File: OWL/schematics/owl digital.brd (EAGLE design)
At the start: 60 x 57 mm, 60 parts, among them IC1 REG1117, IC3 IS61WV51216BLL-10TLI, U2 WM8731, U4 STM32F405ZGT6

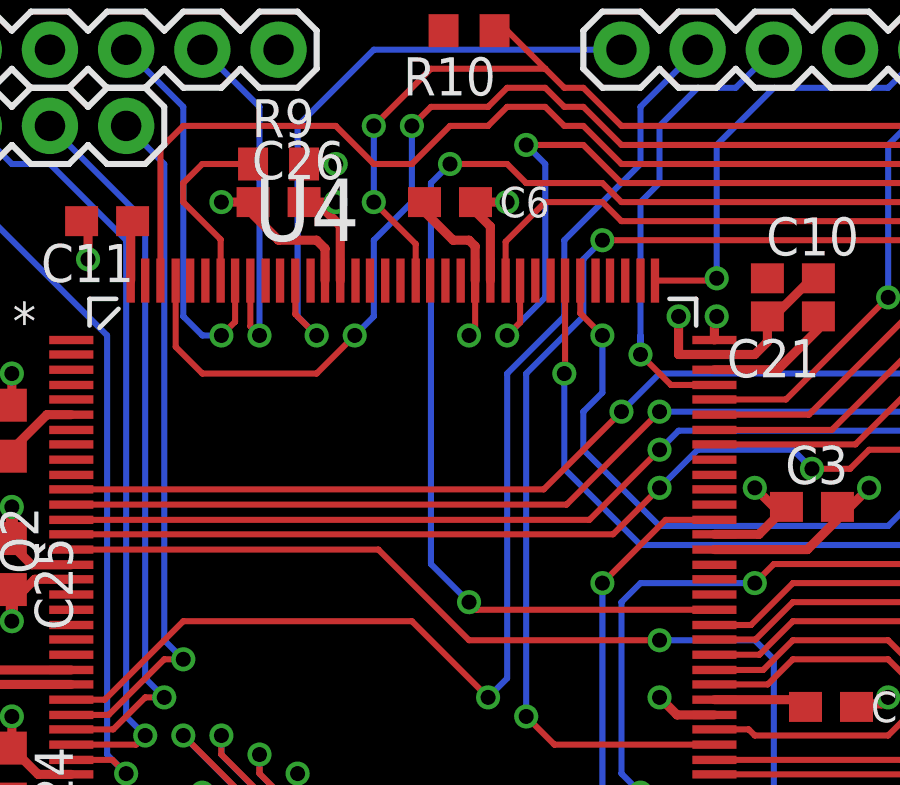
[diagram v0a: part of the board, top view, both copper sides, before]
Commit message: split owl board into analog and digital boards
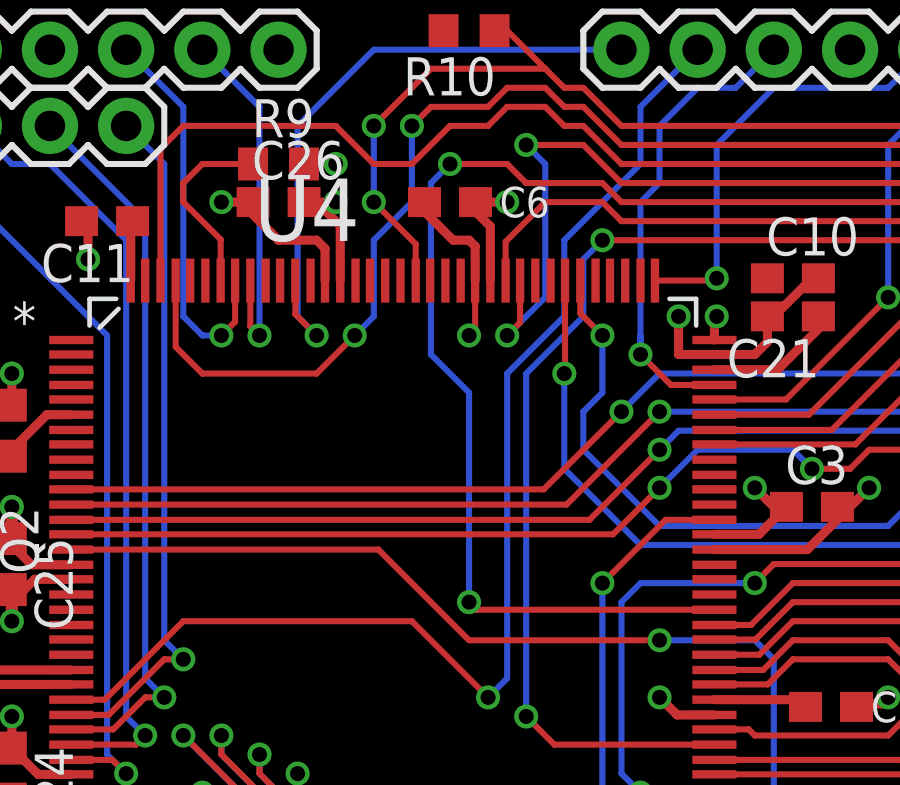
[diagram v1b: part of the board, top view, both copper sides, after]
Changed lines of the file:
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@@
 <contactref element="PWR" pad="3"/>
 <wire x1="19.05" y1="6.35" x2="19.05" y2="4.475" width="0.8128" layer="1"/>
-<wire x1="30.265" y1="47.625" x2="38.1" y2="55.245" width="0" layer="19" extent="1-1"/>
+<wire x1="18.415" y1="3.84" x2="16.54" y2="3.84" width="0.8128" layer="1"/>
+<wire x1="16.54" y1="3.84" x2="16.51" y2="3.81" width="0.8128" layer="1"/>
+<via x="16.51" y="3.81" extent="1-16" drill="0.5"/>
+<wire x1="10.1346" y1="3.8354" x2="12.0396" y2="3.8354" width="0.8128" layer="1"/>
+<wire x1="12.0396" y1="3.8354" x2="12.065" y2="3.81" width="0.8128" layer="1"/>
+<via x="12.065" y="3.81" extent="1-16" drill="0.5"/>
 <wire x1="28.575" y1="46.355" x2="30.265" y2="47.625" width="0" layer="19" extent="1-1"/>
 <wire x1="29.845" y1="40.64" x2="28.4988" y2="45.5676" width="0" layer="19" extent="1-1"/>
@@
 <wire x1="12.7" y1="23.075" x2="15.24" y2="21.375" width="0" layer="19" extent="1-1"/>
 <wire x1="6.35" y1="21.375" x2="10.033" y2="23.5195" width="0" layer="19" extent="1-1"/>
-<wire x1="7.0612" y1="31.0896" x2="10.033" y2="26.1112" width="0" layer="19" extent="1-1"/>
-<wire x1="5.7404" y1="38.0746" x2="5.08" y2="33.02" width="0" layer="19" extent="1-1"/>
-<wire x1="5.08" y1="41.695" x2="5.08" y2="40.005" width="0" layer="19" extent="1-1"/>
-<wire x1="9.0424" y1="47.5488" x2="7.0612" y2="43.0784" width="0" layer="19" extent="1-1"/>
 <wire x1="12.065" y1="50.165" x2="9.105" y2="49.53" width="0" layer="19" extent="1-1"/>
-<wire x1="18.835" y1="49.8475" x2="15.5194" y2="48.6156" width="0" layer="19" extent="1-1"/>
 <wire x1="19.47" y1="55.88" x2="18.835" y2="50.165" width="0" layer="19" extent="1-1"/>
-<wire x1="13.755" y1="13.97" x2="15.24" y2="20.32" width="0" layer="19" extent="1-1"/>
-<wire x1="23.495" y1="13.97" x2="20.955" y2="20.955" width="0" layer="19" extent="1-1"/>
 <wire x1="19.05" y1="6.35" x2="23.28" y2="10.795" width="0" layer="19" extent="1-1"/>
-<wire x1="31.75" y1="6.35" x2="23.28" y2="10.795" width="0" layer="19" extent="1-1"/>
-<wire x1="35.14" y1="3.175" x2="32.805" y2="6.35" width="0" layer="19" extent="1-1"/>
-<wire x1="40.005" y1="6.985" x2="38.19" y2="4.355" width="0" layer="19" extent="1-1"/>
 <wire x1="45.0272" y1="12.155" x2="40.005" y2="11.43" width="0" layer="19" extent="1-1"/>
-<wire x1="43.815" y1="37.045" x2="31.535" y2="33.3375" width="0" layer="19" extent="1-1"/>
-<wire x1="57.67" y1="36.43" x2="47.625" y2="37.465" width="0" layer="19" extent="1-1"/>
-<wire x1="18.415" y1="3.84" x2="16.54" y2="3.84" width="0.8128" layer="1"/>
-<wire x1="16.54" y1="3.84" x2="16.51" y2="3.81" width="0.8128" layer="1"/>
-<via x="16.51" y="3.81" extent="1-16" drill="0.5"/>
-<wire x1="10.1346" y1="3.8354" x2="12.0396" y2="3.8354" width="0.8128" layer="1"/>
-<wire x1="12.0396" y1="3.8354" x2="12.065" y2="3.81" width="0.8128" layer="1"/>
-<via x="12.065" y="3.81" extent="1-16" drill="0.5"/>
-<wire x1="12.065" y1="3.81" x2="16.51" y2="3.81" width="0" layer="19" extent="1-16"/>
+<wire x1="47.625" y1="37.465" x2="57.67" y2="36.43" width="0" layer="19" extent="1-1"/>
+<wire x1="38.1" y1="55.245" x2="30.265" y2="47.625" width="0" layer="19" extent="1-1"/>
 </signal>
 <signal name="SWCLK">
@@
 <wire x1="20.574" y1="36.576" x2="20.32" y2="36.83" width="0.2032" layer="1"/>
 <via x="20.32" y="36.83" extent="1-16" drill="0.5"/>
-<wire x1="20.32" y1="36.83" x2="19.05" y2="38.1" width="0.2032" layer="16"/>
-<wire x1="19.05" y1="38.1" x2="19.05" y2="50.8" width="0.2032" layer="16"/>
+<wire x1="20.32" y1="36.83" x2="20.32" y2="43.815" width="0.2032" layer="16"/>
+<wire x1="20.32" y1="43.815" x2="19.05" y2="45.085" width="0.2032" layer="16"/>
+<wire x1="19.05" y1="45.085" x2="19.05" y2="50.8" width="0.2032" layer="16"/>
 <wire x1="19.05" y1="50.8" x2="19.685" y2="51.435" width="0.2032" layer="16"/>
 <via x="19.685" y="51.435" extent="1-16" drill="0.5"/>

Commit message: latest changes before going 4-layer
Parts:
- USB: device SparkFun:1X04 -> SparkFun:1X05
- moved USB 2.54 mm to (43.2, 55.2)
- renumbered JP3 to ADC
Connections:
- net GND: now also USB.5
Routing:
- net USB_DP: track 29.1 -> 36.3 mm
- net GND: track 121.1 -> 124.5 mm
- net USB_VBUS: track 127.2 -> 124.8 mm
- net +3V3: track 95.9 -> 94.0 mm, vias 22 -> 21
- net PD9: track 51.5 -> 49.8 mm
- net USB_ID: track 42.1 -> 40.4 mm
- net PD10: track 49.0 -> 47.3 mm
- net PD8: track 52.0 -> 50.7 mm
- net PF1: track 41.0 -> 42.1 mm
- net PG10: track 51.2 -> 50.3 mm
- net USB_DM: track 36.0 -> 35.4 mm
- net PF2: track 40.9 -> 41.4 mm
- net PD11: track 45.3 -> 44.7 mm

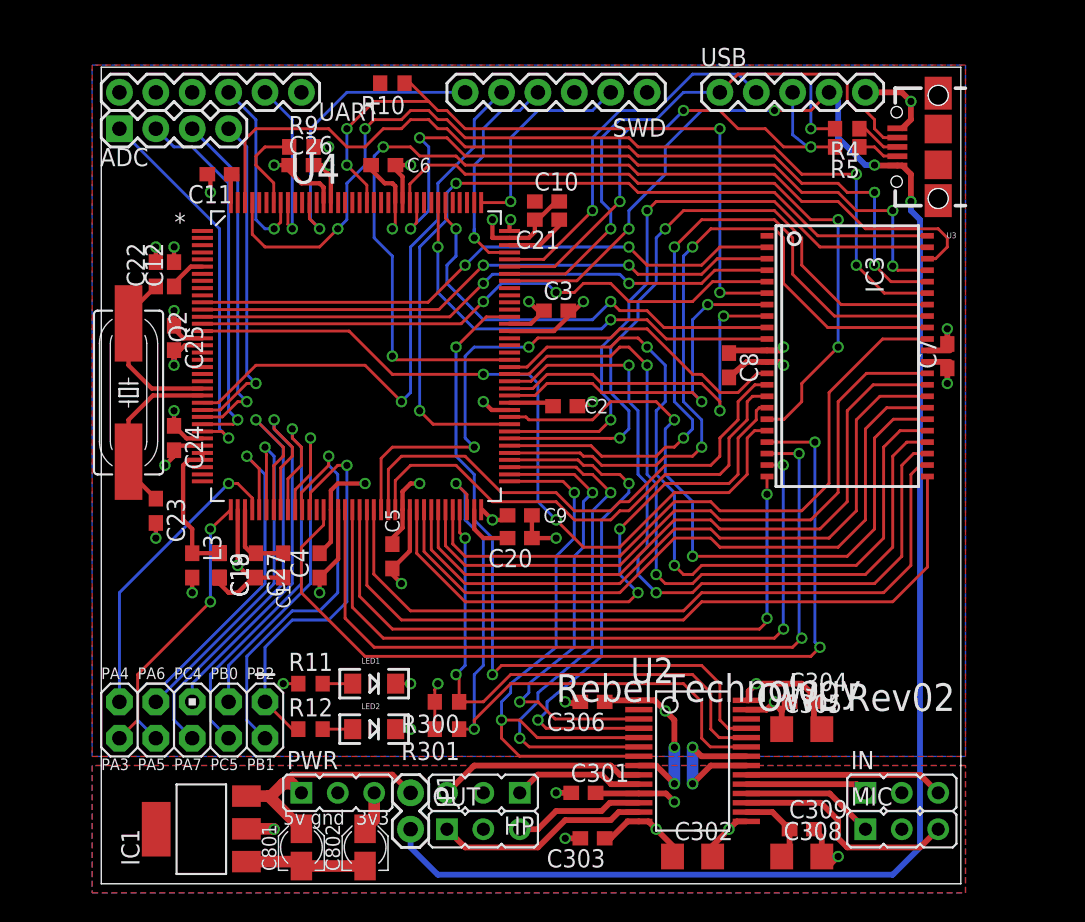
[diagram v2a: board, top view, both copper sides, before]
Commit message: changed to four layers and 0.0125 grid
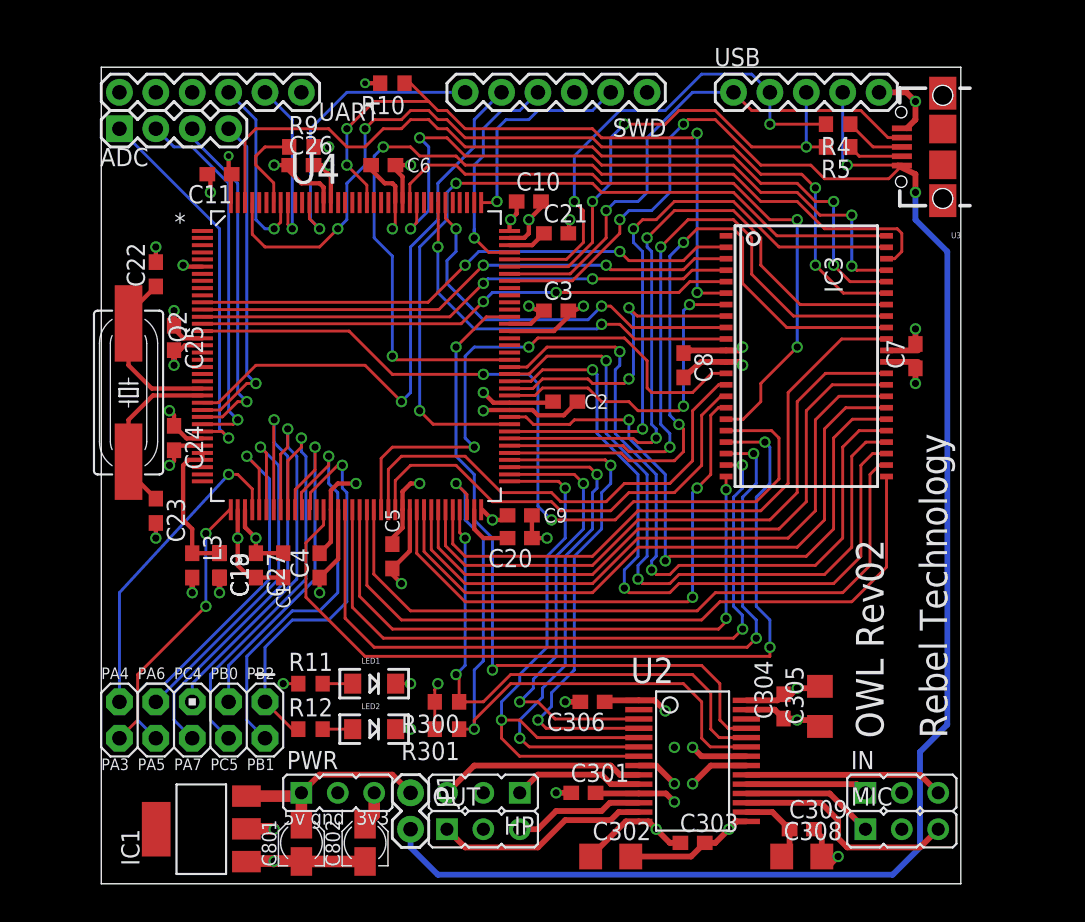
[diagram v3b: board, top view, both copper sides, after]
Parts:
- removed C12: 100n, resistor:C0603
- moved C303 6.99 mm to (41.3, 2.86), turned to 0 degrees
- moved C302 5.71 mm to (35.6, 1.91)
- moved C8 3.17 mm to (40.6, 36.2)
- moved IC3 2.86 mm to (49.2, 36.8)
- moved C7 2.22 mm to (56.8, 36.8)
- moved C305 2.03 mm to (50.2, 12.4), turned to 90 degrees
- moved C304 1.31 mm to (47.6, 12.4), turned to 90 degrees
- moved C10 1.27 mm to (29.8, 47.6)
- moved C21 1.14 mm to (31.8, 45.4), turned to 0 degrees
- moved USB 0.95 mm to (44.1, 55.2)
- moved R4 0.71 mm to (51.4, 53.0)
- moved R5 0.63 mm to (51.4, 51.4)
- moved C2 0.32 mm to (32.4, 33.7)
- moved C801 0.32 mm to (14.0, 2.86)
- moved C802 0.32 mm to (18.4, 2.86)
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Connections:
- net +3V3: no longer C12.1
- net GND: no longer C12.2
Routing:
- net USB_VBUS: track 124.8 -> 134.7 mm
- net PD15: track 26.3 -> 21.1 mm
- net PD13: track 47.3 -> 42.8 mm
- net PF4: track 42.2 -> 37.8 mm
- net +3V3: track 94.0 -> 98.3 mm, vias 21 -> 26
- net PG4: track 53.1 -> 49.5 mm
- net PG3: track 52.8 -> 49.4 mm
- net PG2: track 52.7 -> 49.2 mm
- net PE0: track 65.6 -> 62.2 mm
- net PF3: track 41.3 -> 37.9 mm
- net PD8: track 50.7 -> 47.3 mm
- net PF1: track 42.1 -> 38.7 mm
- net PE15: track 46.4 -> 43.0 mm
- net PE14: track 46.5 -> 43.1 mm
- net PE13: track 47.3 -> 43.9 mm
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- added copper zone on layer 15, net +3V3
- added copper zone on layer 2, net GND
- removed copper zone on layer 1, net +3V3
- removed copper zone on layer 16, net GND

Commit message: updated usb connector part
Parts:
- removed U3: (no value), SparkFun-Connectors:USB-AB-MICRO-SMD
- added USB1: (no value), USB_connector:HRS_ZX62D-AB-5P8_USB
- moved R4 0.95 mm to (50.5, 53.0)
- moved R5 0.95 mm to (50.5, 51.4)
- moved USB 0.32 mm to (44.5, 55.2)
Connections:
- net GND: now also USB1.5, USB1.G, USB1.G2, USB1.G3, USB1.G4; no longer U3.GND
- net N$17: now also USB1.3; no longer U3.D+
- net N$21: now also USB1.2; no longer U3.D-
- net USB_ID: now also USB1.4; no longer U3.ID
- net USB_VBUS: now also USB1.1; no longer U3.VBUS
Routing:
- net USB_VBUS: track 134.7 -> 131.6 mm, vias 4 -> 3
- net GND: track 121.8 -> 119.9 mm, vias 30 -> 29
- net N$17: track 4.26 -> 5.28 mm
- net N$21: track 3.88 -> 4.90 mm
- net USB_DP: track 34.6 -> 33.7 mm

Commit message: routing updates
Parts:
- moved R10 1.42 mm to (19.7, 54.6)
- moved SWD 1.27 mm to (36.8, 55.2)
- moved C6 0.64 mm to (20.3, 50.2)
- moved C8 0.32 mm to (41.0, 36.2)
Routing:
- net PD4: track 47.6 -> 42.4 mm
- net GND: track 119.9 -> 117.9 mm
- net PG10: track 47.5 -> 45.8 mm
- net +3V3: track 98.2 -> 96.6 mm
- net SWDIO: track 16.3 -> 15.0 mm
- net SWCLK: track 15.2 -> 13.9 mm
- net PD5: track 47.1 -> 46.1 mm
- net PE0: track 62.2 -> 61.2 mm
- net SWO: track 21.2 -> 20.4 mm
- net NRST: track 40.6 -> 39.8 mm
- net ADC3: track 26.0 -> 25.3 mm
- net PB2: track 27.8 -> 28.6 mm
- net USB_DP: track 33.7 -> 33.0 mm, vias 2 -> 3
- net I2C_SDA: track 45.4 -> 44.8 mm
- net PE1: track 58.1 -> 57.5 mm
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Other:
- board size 60 x 57 mm -> 60 x 56.3 mm
